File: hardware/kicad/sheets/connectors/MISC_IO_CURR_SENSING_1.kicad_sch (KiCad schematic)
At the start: 20 parts

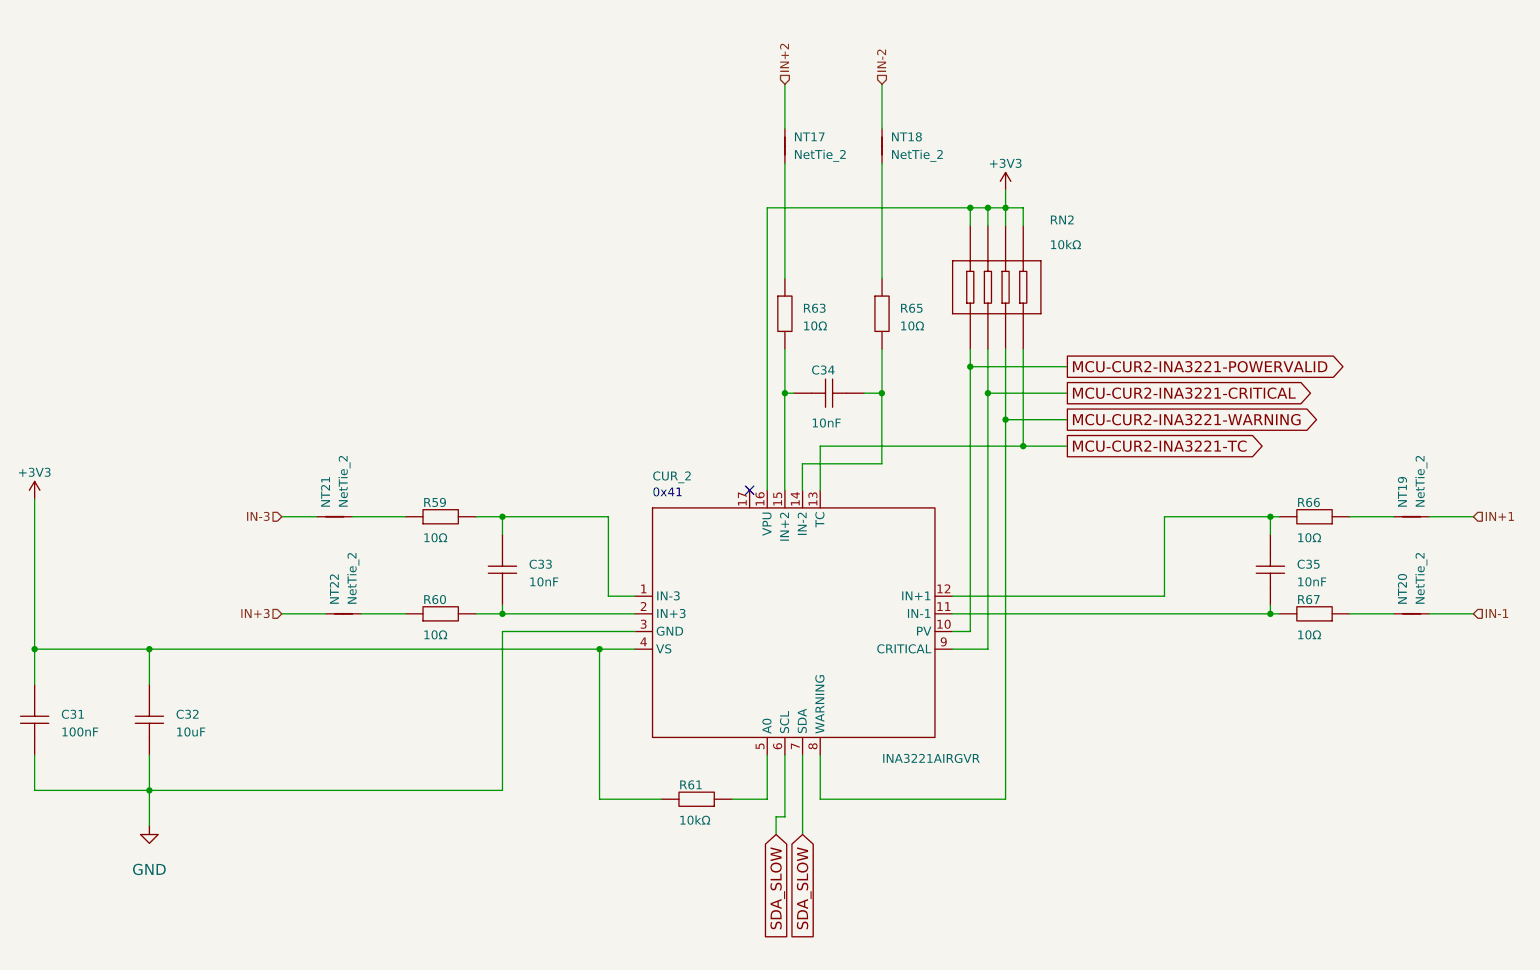
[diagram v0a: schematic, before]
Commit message: sheet optimized ports and current sensor
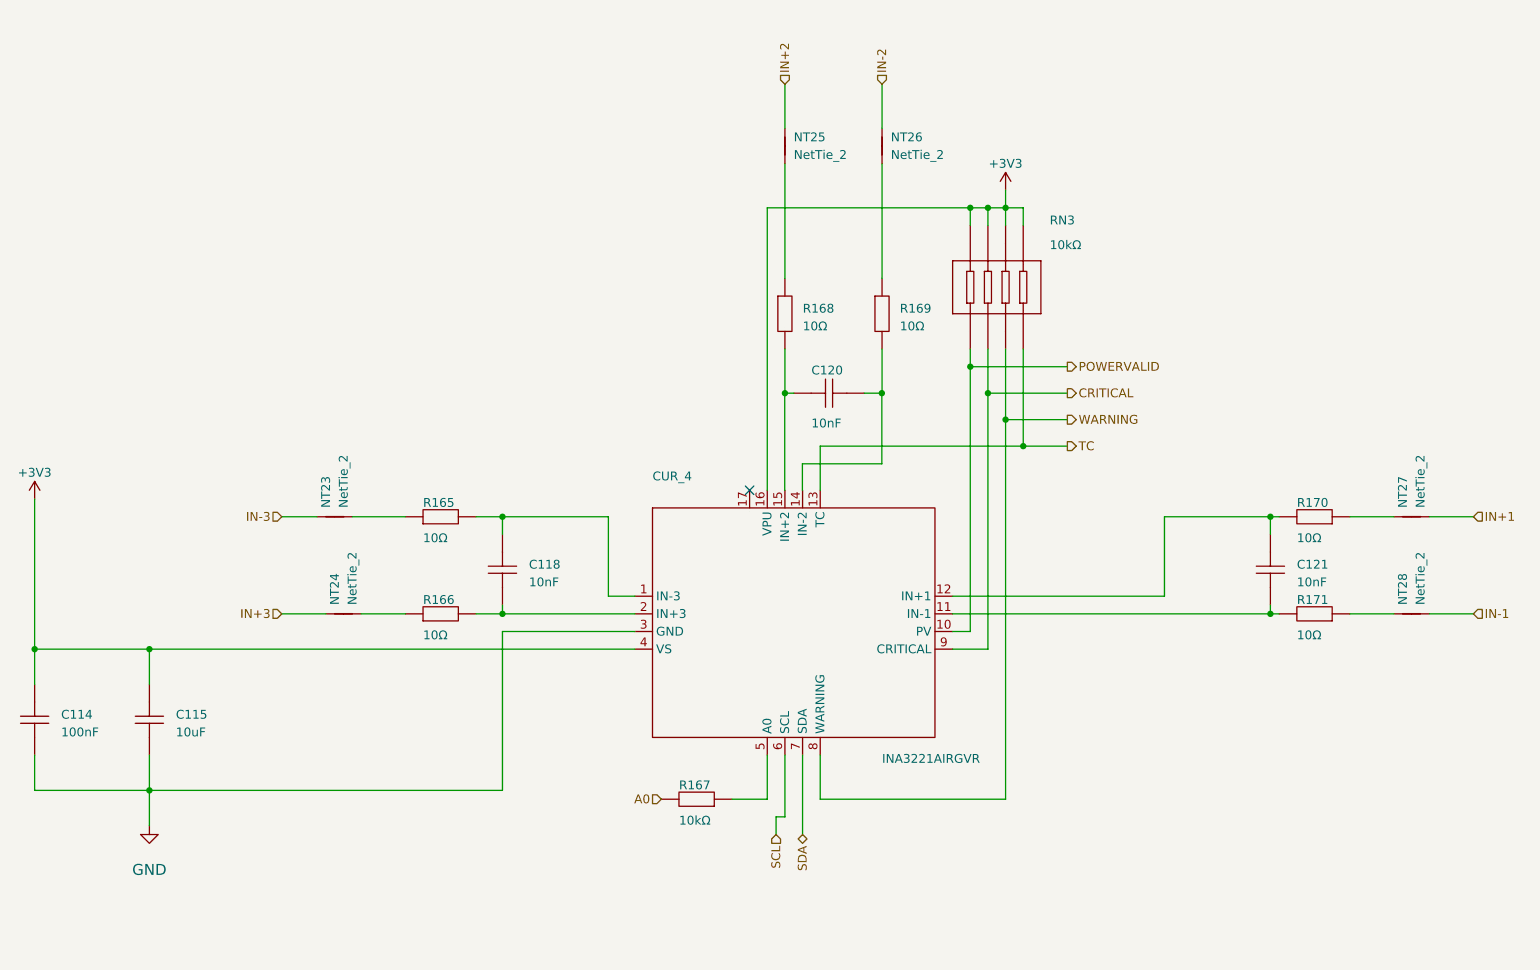
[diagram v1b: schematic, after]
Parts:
- renumbered C31 to C114, C32 to C115, C33 to C118, C34 to C120, C35 to C121, CUR_2 to CUR_4, NT21 to NT23, NT22 to NT24, NT17 to NT25, NT18 to NT26, NT19 to NT27, NT20 to NT28, R59 to R165, R60 to R166, R61 to R167, R63 to R168, R65 to R169, R66 to R170, R67 to R171, RN2 to RN3
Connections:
- net +3V3: no longer R167.2
- net MCU-CUR2-INA3221-CRITICAL renamed CRITICAL
- net MCU-CUR2-INA3221-POWERVALID renamed POWERVALID
- net MCU-CUR2-INA3221-TC renamed TC
- net MCU-CUR2-INA3221-WARNING renamed WARNING
- net SDA_SLOW renamed SCL
- net SCL: no longer CUR_4.7 (SDA)
- new net A0: R167.2
- new net SDA: CUR_4.7 (SDA)
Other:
- note removed: "0x41"

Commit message: more sheet simplfiication and pre simpler 12v sym
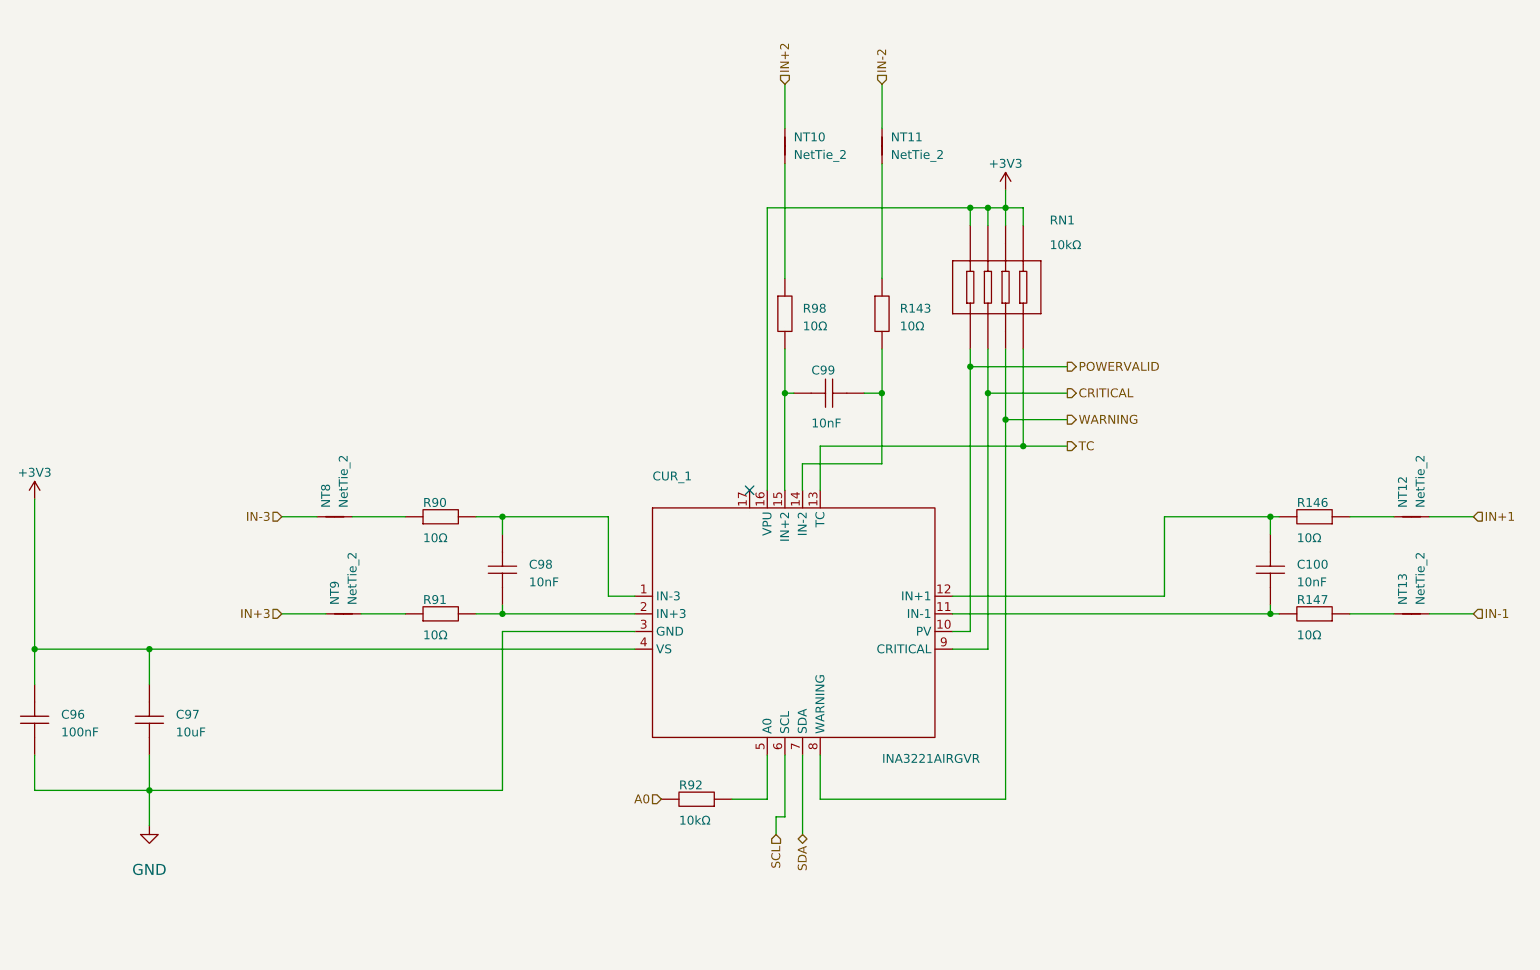
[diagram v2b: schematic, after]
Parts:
- renumbered C121 to C100, C114 to C96, C115 to C97, C118 to C98, C120 to C99, CUR_4 to CUR_1, NT25 to NT10, NT26 to NT11, NT27 to NT12, NT28 to NT13, NT23 to NT8, NT24 to NT9, R169 to R143, R170 to R146, R171 to R147, R165 to R90, R166 to R91, R167 to R92, R168 to R98, RN3 to RN1

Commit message: resheeted bms and fixed links for the 12v buck
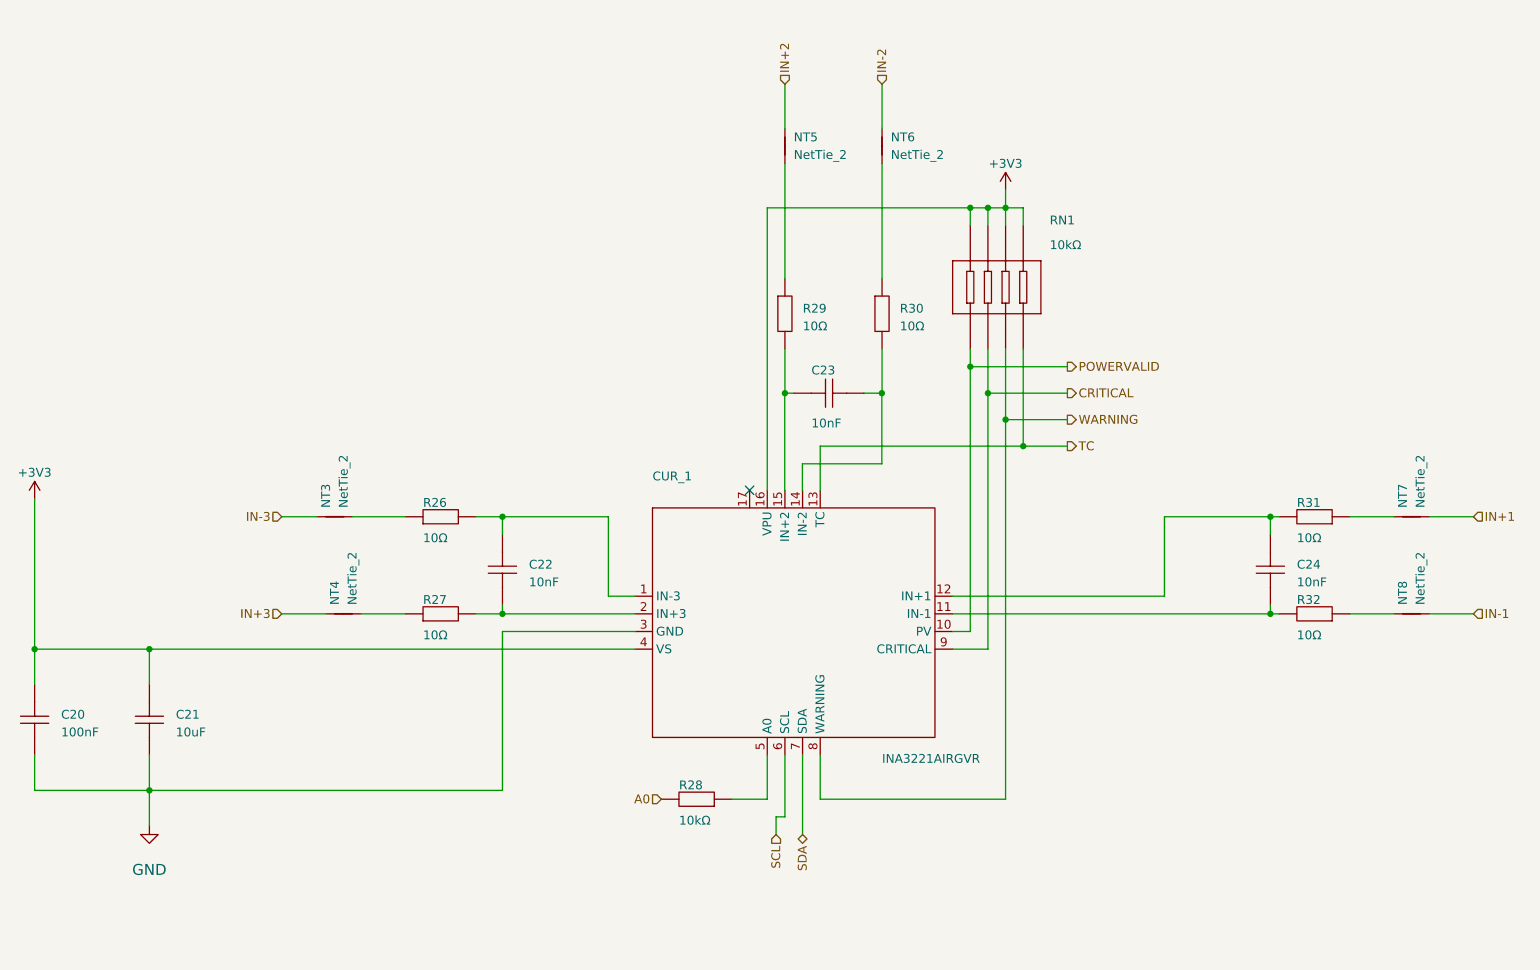
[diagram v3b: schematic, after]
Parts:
- renumbered C96 to C20, C97 to C21, C98 to C22, C99 to C23, C100 to C24, NT8 to NT3, NT9 to NT4, NT10 to NT5, NT11 to NT6, NT12 to NT7, NT13 to NT8, R90 to R26, R91 to R27, R92 to R28, R98 to R29, R143 to R30, R146 to R31, R147 to R32

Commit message: various improvements
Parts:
- renumbered C20 to C24, C21 to C25, C22 to C26, C23 to C27, C24 to C28, NT8 to NT10, NT3 to NT5, NT4 to NT6, NT5 to NT7, NT6 to NT8, NT7 to NT9, R26 to R28, R27 to R29, R28 to R30, R29 to R31, R30 to R32, R31 to R33, R32 to R34
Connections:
- net IN_1_P: now reaches NT9.2, R33.1
- net IN_1_N: now reaches NT10.2, R34.1
- net IN_2_N: now reaches NT8.1, R32.1
- net IN_2_P: now reaches NT7.1, R31.1
- net IN_3_P: now reaches NT6.1, R29.1
- net IN_3_N: now reaches NT5.1, R28.1

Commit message: various improvements
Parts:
- renumbered C24 to C31, C25 to C32, C26 to C33, C27 to C34, C28 to C35, NT9 to NT10, NT10 to NT11, NT5 to NT6, NT6 to NT7, NT7 to NT8, NT8 to NT9, R28 to R37, R29 to R38, R30 to R39, R31 to R40, R32 to R41, R33 to R42, R34 to R43
